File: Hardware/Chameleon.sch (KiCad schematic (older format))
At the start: 59 parts, among them IC1 ATTINY44-SS, P1 CONN_3X2, U1 PCA9685, U2 USBMICRO-B, U3 NCP1402, X1 CRYSTAL

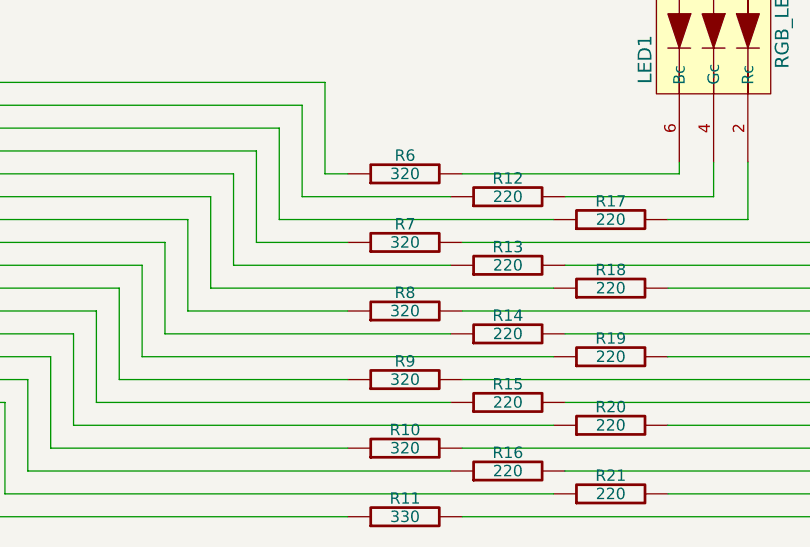
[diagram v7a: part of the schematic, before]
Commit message: Updated BOM, renamed CS1 to C14, Improved firmware slightly
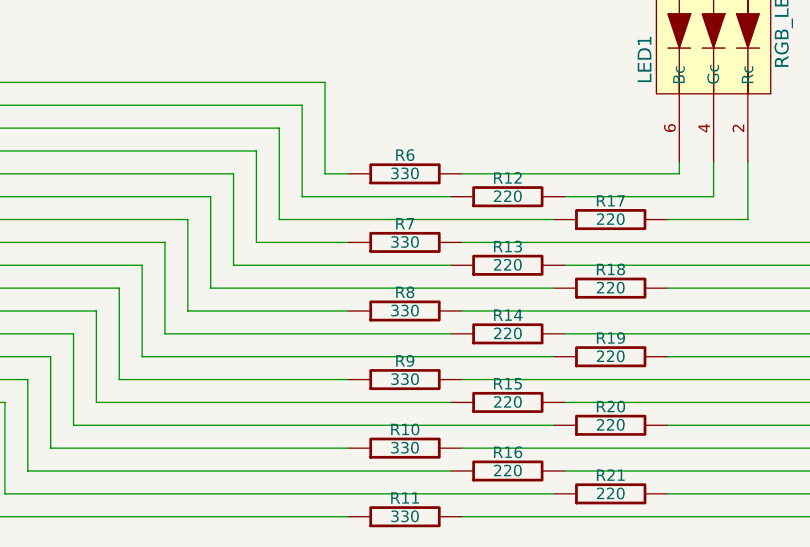
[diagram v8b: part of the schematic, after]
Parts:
- R10, R6, R7, R8, R9: value 320 -> 330
- renumbered CS1 to C14
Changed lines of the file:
@@
-EESchema Schematic File Version 2  date 8/13/2012 5:06:37 PM
+EESchema Schematic File Version 2  date 8/15/2012 11:14:33 PM
 LIBS:power
 LIBS:device
@@
 Sheet 1 1
 Title "Chameleon Drink Coasters"
-Date "13 aug 2012"
+Date "16 aug 2012"
 Rev "1.0"
 Comp "Projects and Stuff LLC"
@@
 $EndComp
 $Comp
-L CSMALL CS1
+L CSMALL C14
 U 1 1 4FA82A80
 P 8650 3450
-F 0 "CS1" H 8675 3500 30  0000 L CNN
+F 0 "C14" H 8675 3500 30  0000 L CNN
 F 1 "10uF" H 8675 3400 30  0000 L CNN
 	1    8650 3450
@@
 P 5750 6700
 F 0 "R10" V 5830 6700 50  0000 C CNN
-F 1 "320" V 5750 6700 50  0000 C CNN
+F 1 "330" V 5750 6700 50  0000 C CNN
 	1    5750 6700
 	0    -1   -1   0
@@
 P 5750 5500
 F 0 "R6" V 5830 5500 50  0000 C CNN
-F 1 "320" V 5750 5500 50  0000 C CNN
+F 1 "330" V 5750 5500 50  0000 C CNN
 	1    5750 5500
 	0    -1   -1   0
@@
 P 5750 5800
 F 0 "R7" V 5830 5800 50  0000 C CNN
-F 1 "320" V 5750 5800 50  0000 C CNN
+F 1 "330" V 5750 5800 50  0000 C CNN
 	1    5750 5800
 	0    -1   -1   0
@@
 P 5750 6400
 F 0 "R9" V 5830 6400 50  0000 C CNN
-F 1 "320" V 5750 6400 50  0000 C CNN
+F 1 "330" V 5750 6400 50  0000 C CNN
 	1    5750 6400
 	0    -1   -1   0
@@
 P 5750 6100
 F 0 "R8" V 5830 6100 50  0000 C CNN
-F 1 "320" V 5750 6100 50  0000 C CNN
+F 1 "330" V 5750 6100 50  0000 C CNN
 	1    5750 6100
 	0    -1   -1   0
@@
 6E 56 52 49 51 4E 59 71 7E 65 C5 4D 0F AF 00 BF F6 21 9D BA 45 88 9C 00 16 00 C0 66 90 E0 00 00
 AC 42 3B 38 00 00 AB 90 E0 00 00 AC 42 82 03 00 B0 EA FF 00 E3 76 B5 A7 81 B6 BC 08 00 00 00 00
-49 45 4E 44 AE 42 60 82 E8 $EndBitmap
+49 45 4E 44 AE 42 60 82 FD $EndBitmap
 EndData
 $EndBitmap
